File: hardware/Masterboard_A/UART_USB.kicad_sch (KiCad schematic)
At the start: 7 parts, among them J16 USB_B_Micro, U1 ISO7721D, U12 FT230XS, U8 L78L05_SOT89

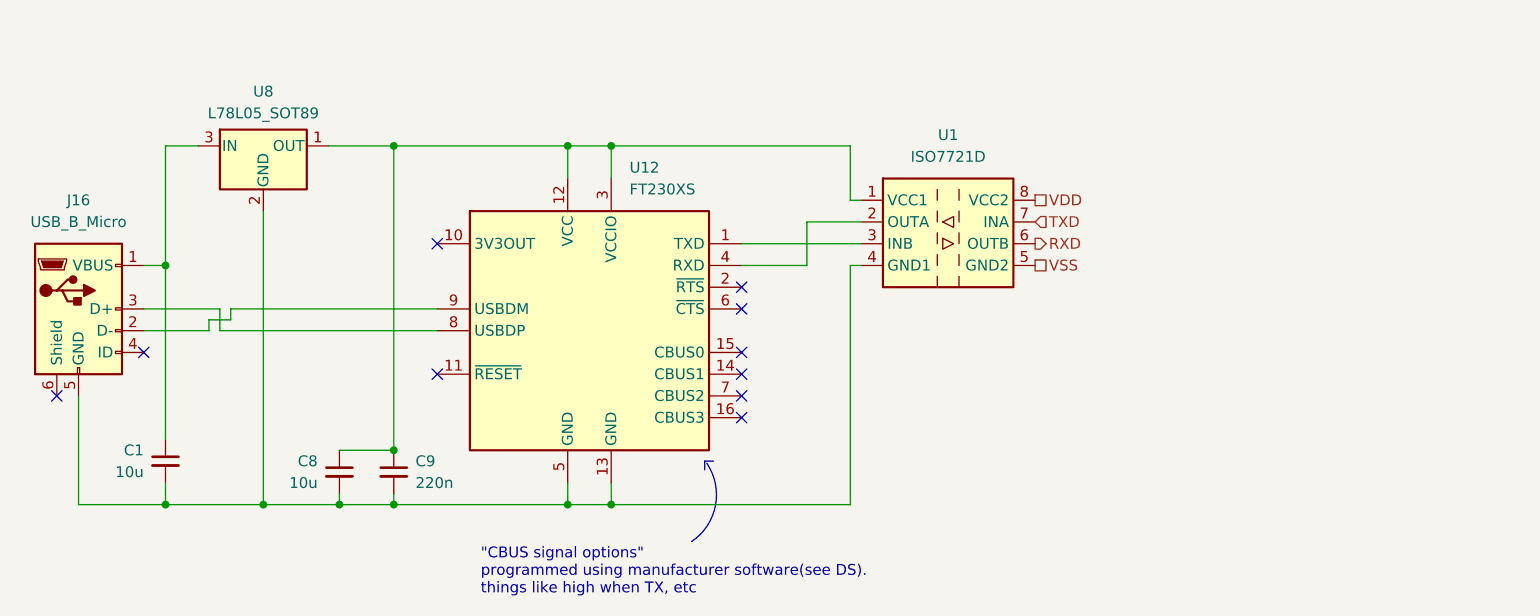
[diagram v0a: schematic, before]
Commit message: basic psu for master board
we scrapping the onboard HRLV supply. solution is "thats not our problem", if they dont want HV on the LV then they should isolate it, not us.
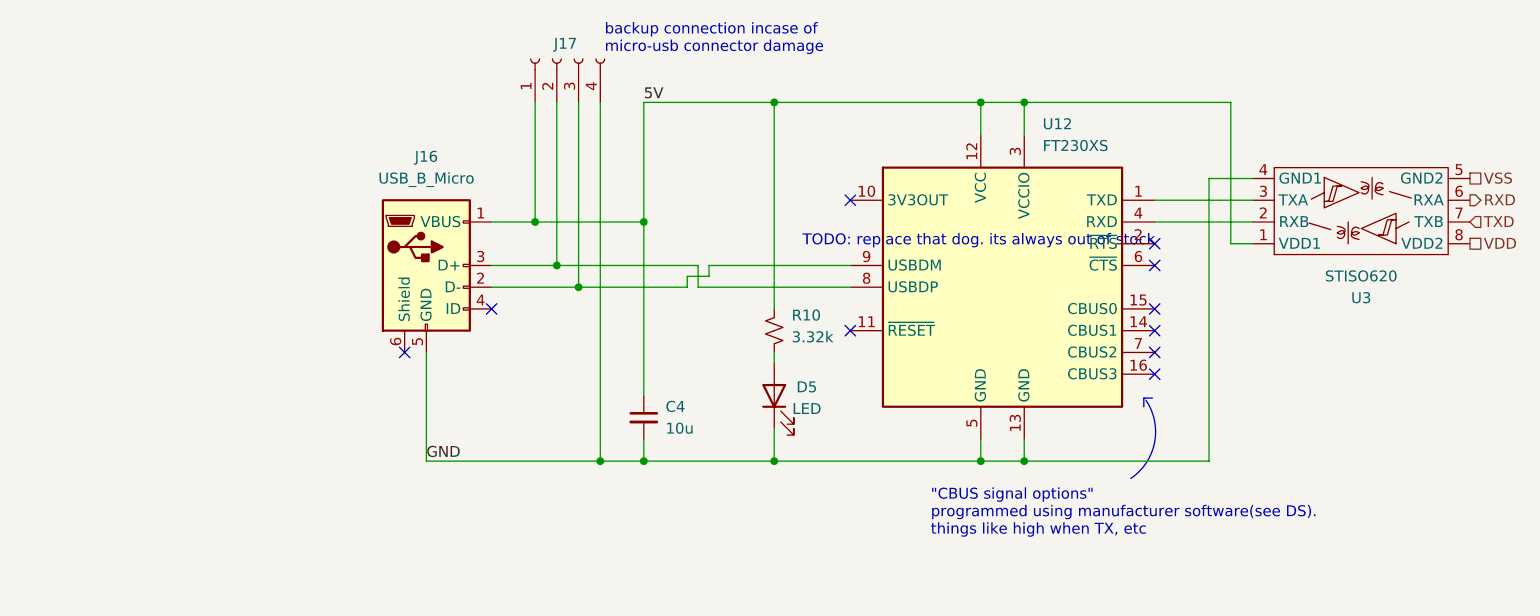
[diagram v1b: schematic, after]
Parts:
- removed C1, C8: 10u, Capacitor_SMD:C_1206_3216Metric_Pad1.33x1.80mm_HandSolder, symbol Device:C_Small
- removed C9: 220n, Capacitor_SMD:C_1206_3216Metric_Pad1.33x1.80mm_HandSolder, symbol Device:C_Small
- removed U1: ISO7721D, Package_SO:SOIC-8_3.9x4.9mm_P1.27mm, symbol Isolator:ISO7721D
- removed U8: L78L05_SOT89, Package_TO_SOT_SMD:SOT-89-3, symbol Regulator_Linear:L78L05_SOT89
- added C4: 10u, Capacitor_SMD:C_1206_3216Metric_Pad1.33x1.80mm_HandSolder, symbol Device:C_Small
- added D5: LED, LED_SMD:LED_0603_1608Metric, symbol Device:LED
- added J17: Conn_01x04_Socket, Connector_PinHeader_2.54mm:PinHeader_1x04_P2.54mm_Vertical, symbol Connector:Conn_01x04_Socket
- added R10: 3.32k, Resistor_SMD:R_0805_2012Metric_Pad1.20x1.40mm_HandSolder, symbol Device:R_Small_US
- added U3: STISO620, Package_SO:SOIC-8_7.5x5.85mm_P1.27mm, symbol zzLocalLibrary:STISO621
- U12: note (none) -> https://www.eevblog.com/forum/reviews/alternatives-to-ftdi-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
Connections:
- net RXD: now also U3.6 (RXA)
- net TXD: now also U3.7 (TXB)
- net VDD: now also U3.8 (VDD2)
- net VSS: now also U3.5 (GND2)
- net 5V: now reaches U12.12 (VCC), U12.3 (VCCIO)
- net 5V: now also J16.1 (VBUS), C4.1, J17.1 (Pin_1), R10.2, U3.1 (VDD1)
- net GND: now reaches J16.5 (GND), U12.13 (GND), U12.5 (GND)
- net GND: now also C4.2, D5.1 (K), J17.4 (Pin_4), U3.4 (GND1)
- net at J16.2 (D-), U12.9 (USBDM): now also J17.3 (Pin_3)
- net at J16.3 (D+), U12.8 (USBDP): now also J17.2 (Pin_2)
- net at U12.4 (RXD): now also U3.2 (RXB)
- net at U12.1 (TXD): now also U3.3 (TXA)
- new net: D5.2 (A), R10.1
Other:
- note added: "TODO: replace that dog. its always out of stock"
- note added: "backup connection incase of micro-usb connector damage"
- moved on the sheet: J16, U12
